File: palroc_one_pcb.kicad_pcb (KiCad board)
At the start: 6 copper layers, 1 part, among them U1 ME54BS13_V1.0

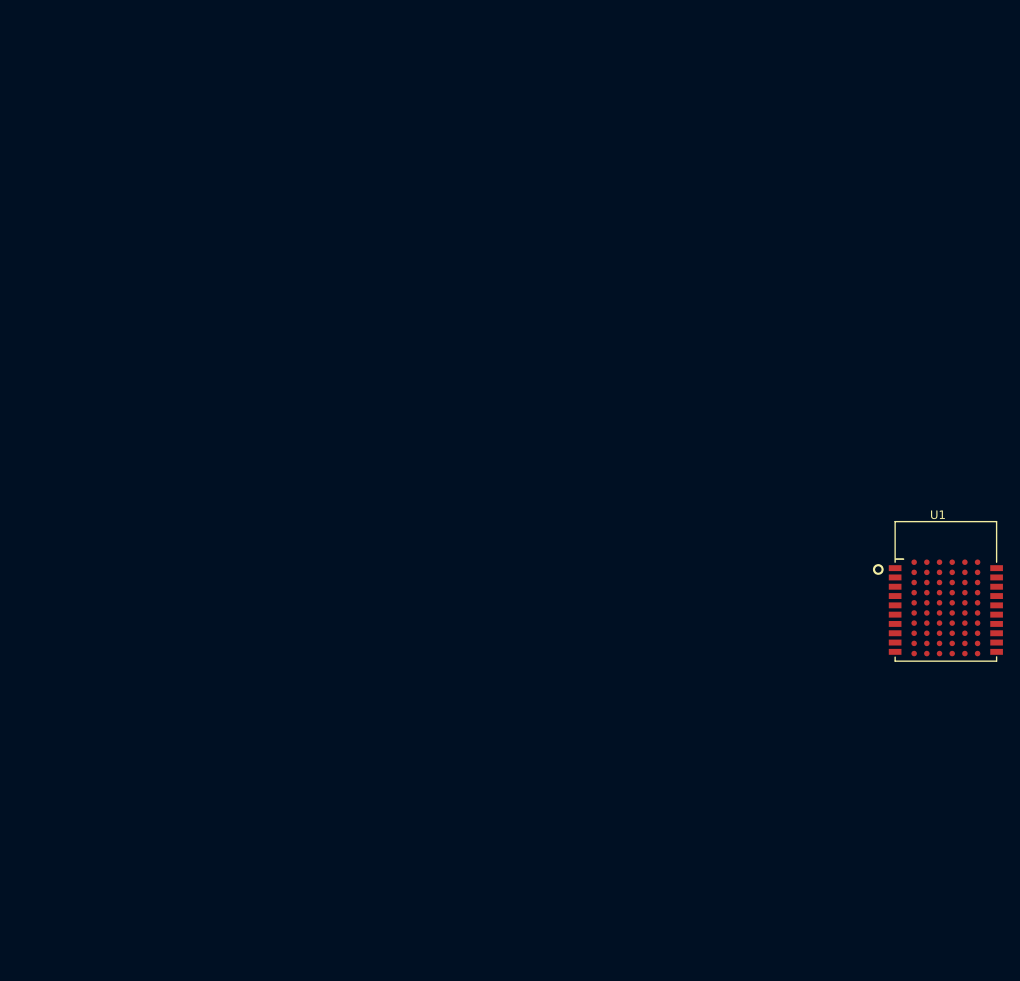
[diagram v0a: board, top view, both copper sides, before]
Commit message: Add power supply, connectors, LoRa, gas sensor, audio, and display sheets
Adds nPM1300 power management, USB-C connectors, Minew LoRa module,
multi-gas sensing (CO2/particulate), audio, and display schematics
along with the supporting component libraries and updated PCB routing.

Co-Authored-By: Claude Sonnet 5 <noreply@anthropic.com>
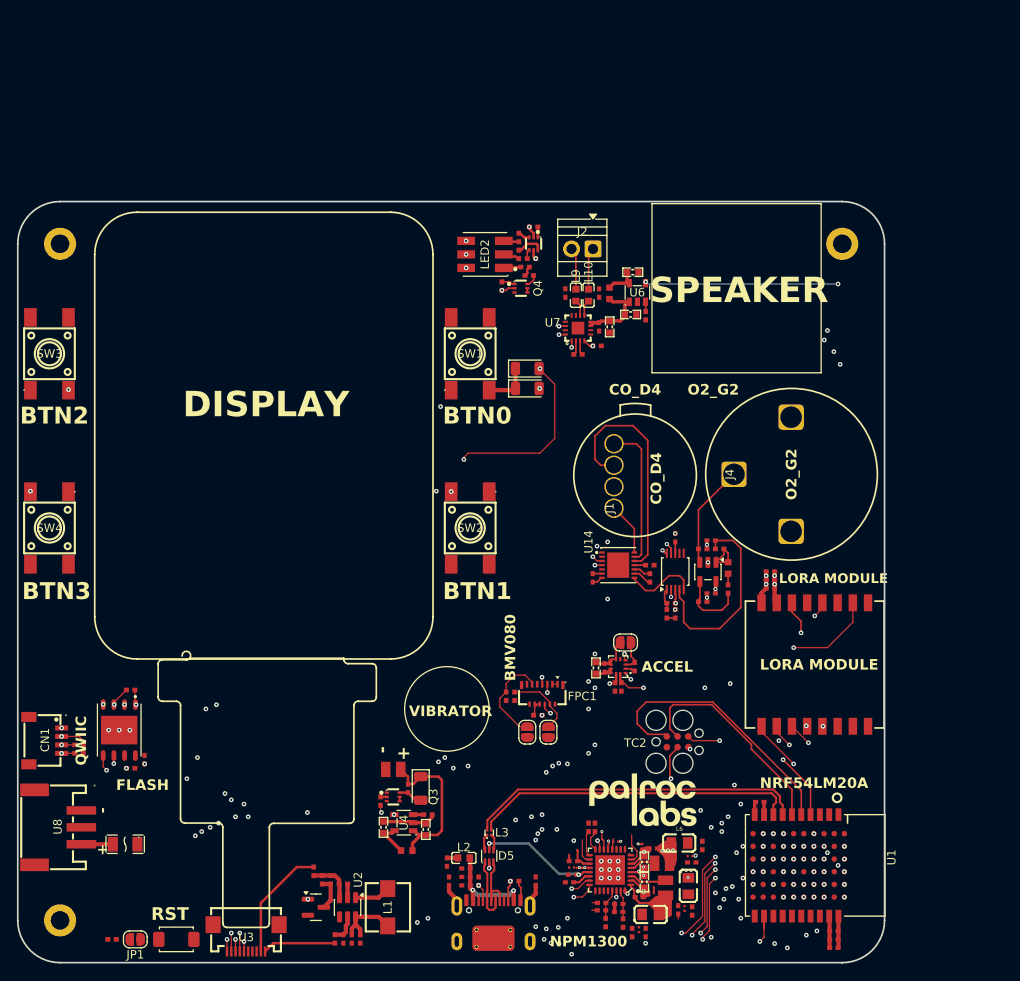
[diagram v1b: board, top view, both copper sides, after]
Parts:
- added C1: 10nF, caps_nordic:c_0402_nordic, F.Cu at (135.2, 128.2)
- added C10: 10nF, caps_nordic:c_0402_nordic, F.Cu at (89.8, 122.4)
- added C11: 10nF, caps_nordic:c_0402_nordic, F.Cu at (91.8, 122.9)
- added C12: 100nF, caps_nordic:c_0402_nordic, F.Cu at (91.8, 121.9)
- added C13: 1uF, caps_nordic:c_0402_nordic, F.Cu at (91.8, 120.9)
- added C14: 100nF, caps_nordic:c_0402_nordic, F.Cu at (89.5, 120.1)
- added C15: 1uF, caps_nordic:c_0402_nordic, F.Cu at (104.3, 121.6)
- added C16: 2.2uF, caps_nordic:c_0402_nordic, F.Cu at (104.5, 120.0)
- added C17: 100nF, caps_nordic:c_0201_nordic, F.Cu at (109.5, 117.7)
- added C18: 10uF, caps_nordic:c_0603_nordic, F.Cu at (112.8, 122.5)
- added C19: 10uF, caps_nordic:c_0402_nordic, F.Cu at (109.8, 125.1)
- added C2: 100nF, caps_nordic:c_0402_nordic, F.Cu at (135.2, 129.2)
- added C20: 1nF, caps_nordic:c_0201_nordic, F.Cu at (113.7, 123.7)
- added C21: 10uF, caps_nordic:c_0402_nordic, F.Cu at (112.2, 124.3)
- added C22: 10uF, caps_nordic:c_0402_nordic, F.Cu at (113.9, 118.5)
- added C23: 10uF, caps_nordic:c_0402_nordic, F.Cu at (109.8, 126.0)
- added C24: 10uF, caps_nordic:c_0603_nordic, F.Cu at (112.8, 120.1)
- added C25: 1nF, caps_nordic:c_0201_nordic, F.Cu at (112.6, 118.3)
- added C26: 1nF, caps_nordic:c_0201_nordic, F.Cu at (104.2, 120.8)
- added C27: 10uF, caps_nordic:c_0402_nordic, F.Cu at (107.8, 124.9)
- added C28: 10uF, caps_nordic:c_0402_nordic, F.Cu at (113.0, 128.5)
- added C29: 10uF, caps_nordic:c_0402_nordic, F.Cu at (118.5, 120.2)
- added C3: 1uF, caps_nordic:c_0402_nordic, F.Cu at (135.2, 130.2)
- added C30: 10uF, caps_nordic:c_0402_nordic, F.Cu at (116.8, 125.8)
- added C31: 10uF, caps_nordic:c_0402_nordic, F.Cu at (107.8, 125.8)
- added C32: 100pF, caps_nordic:c_0201_nordic, F.Cu at (112.2, 128.1)
- added C33: 100pF, caps_nordic:c_0201_nordic, F.Cu at (117.6, 125.6)
- added C34: 100pF, caps_nordic:c_0201_nordic, F.Cu at (118.2, 119.4)
- added C35: 1uF, caps_nordic:c_0402_nordic, F.Cu at (104.0, 122.5)
- added C36: 10uF, caps_nordic:c_0603_nordic, F.Cu at (108.8, 56.8)
- added C37: 100nF, caps_nordic:c_0402_nordic, F.Cu at (107.5, 56.8)
- added C38: 220pF, caps_nordic:c_0402_nordic, F.Cu at (103.5, 52.8)
- added C39: 220pF, caps_nordic:c_0402_nordic, F.Cu at (107.5, 52.8)
- added C4: 10nF, caps_nordic:c_0402_nordic, F.Cu at (127.8, 87.8)
- added C40: 100nF, caps_nordic:c_0402_nordic, F.Cu at (84.9, 111.4)
- added C41: 1uF, caps_nordic:c_0402_nordic, F.Cu at (126.5, 113.0)
- added C42: 100nF, caps_nordic:c_0402_nordic, F.Cu at (53.8, 108.0)
- added C43: 10uF, caps_nordic:c_0603_nordic, F.Cu at (82.0, 116.0)
- added C44: 10uF, caps_nordic:c_0603_nordic, F.Cu at (87.0, 116.2)
- added C45: 10uF, caps_nordic:c_0603_nordic, F.Cu at (111.5, 50.4)
- added C46: 10uF, caps_nordic:c_0603_nordic, F.Cu at (111.2, 55.4)
- added C47: 10uF, caps_nordic:c_0603_nordic, F.Cu at (107.1, 97.1)
- added C48: 100nF, caps_nordic:c_0402_nordic, F.Cu at (108.1, 97.1)
- added C49: 100nF, caps_nordic:c_0402_nordic, F.Cu at (116.5, 81.8)
- added C5: 100nF, caps_nordic:c_0402_nordic, F.Cu at (127.8, 86.8)
- added C50: 100nF, caps_nordic:c_0402_nordic, F.Cu at (120.8, 88.3)
- added C51: 100nF, caps_nordic:c_0402_nordic, F.Cu at (106.8, 86.5)
- added C52: 100nF, caps_nordic:c_0402_nordic, F.Cu at (120.8, 82.1)
- added C6: 1uF, caps_nordic:c_0402_nordic, F.Cu at (127.8, 85.8)
- added C7: 1uF, caps_nordic:c_0402_nordic, F.Cu at (78.2, 129.2)
- added C8: 220pF, caps_nordic:c_0402_nordic, F.Cu at (77.2, 129.2)
- added C9: 10nF, caps_nordic:c_0402_nordic, F.Cu at (100.0, 122.4)
- added CN1: SM04B-SRSS-TB, PALROC_Connectorss:CONN-SMD_4P-P1.00_SM04B-SRSS-TB-LF-SN, F.Cu at (42.0, 105.8)
- added D2: 1N4001W, PCM_JLCPCB:D_SOD-123FL, F.Cu at (86.4, 111.4)
- added D3: 1N4001W, PCM_JLCPCB:D_SOD-123FL, F.Cu at (99.0, 61.8)
- added D4: 1N4001W, PCM_JLCPCB:D_SOD-123FL, F.Cu at (99.0, 64.1)
- added D5: USBLC6-2P6, PALROC-Protection:SOT-666-6_L1.6-W1.2-P0.50-LS1.6-BR, F.Cu at (94.5, 119.4)
- added FPC1: 046844713002846+_C5857733, PALROC_Connectorss:FPC-SMD_13P-P0.60_046844713002846-1, F.Cu at (100.8, 100.3)
- added G***: LOGO, PALROC_Logos:Palroc_Logo_15x15mm, F.Cu at (112.8, 112.8)
- added H1: MountingHole_Pad, MountingHole:MountingHole_2.2mm_M2_DIN965_Pad, F.Cu at (136.2, 47.0)
- added H2: MountingHole_Pad, MountingHole:MountingHole_2.2mm_M2_DIN965_Pad, F.Cu at (43.8, 127.0)
- added H3: MountingHole_Pad, MountingHole:MountingHole_2.2mm_M2_DIN965_Pad, F.Cu at (43.8, 47.0)
- added J1: Conn_01x04, Connector_GasSensors:0294-0-15-80-06-80-10-0_co-d4, F.Cu at (109.2, 78.3)
- added J2: Screw_Terminal_01x02, TerminalBlock:TerminalBlock_Xinya_XY308-2.54-2P_1x02_P2.54mm_Horizontal, F.Cu at (106.8, 47.6)
- added J3: Connector, USB-TYPE-C-16P, PCM_JLCPCB:TYPE-C-SMD_HX-TYPE-C-16PIN, F.Cu at (95.0, 127.1)
- added J4: Conn_01x03, Connector_GasSensors:0364-0-15-80-13-80-10-0_o2-g2, F.Cu at (123.5, 74.2)
- added JP1: SolderJumper_2_Open, Jumper:SolderJumper-2_P1.3mm_Open_RoundedPad1.0x1.5mm, F.Cu at (52.6, 129.2)
- added JP2: SolderJumper_2_Open, Jumper:SolderJumper-2_P1.3mm_Open_RoundedPad1.0x1.5mm, F.Cu at (101.5, 104.8)
- added JP3: SolderJumper_2_Open, Jumper:SolderJumper-2_P1.3mm_Open_RoundedPad1.0x1.5mm, F.Cu at (99.0, 104.8)
- added JP4: SolderJumper_2_Open, Jumper:SolderJumper-2_P1.3mm_Open_RoundedPad1.0x1.5mm, F.Cu at (110.6, 94.1)
- added L1: CXP0530-220M-AG(22UH), PALROC-inductors:IND-SMD_L5.7-W5.2, F.Cu at (82.5, 125.5)
- added L10: BLM18PG471SN1D, PALROC-ferrite-bread:L0603, F.Cu at (106.2, 53.1)
- added L2: BLM18KG121TN1D, PALROC-ferrite-bread:L0603, F.Cu at (91.5, 119.6)
- added L3: DLM0NSN900HY2D, PALROC-Filters:FILTER-SMD_4P-L0.9-W0.7-P0.50-BL-CW, F.Cu at (94.5, 116.6)
- added L4: 2.2uH, l_nordic:l_0806_nordic, F.Cu at (115.3, 123.2)
- added L5: 2.2uH, l_nordic:l_0806_nordic, F.Cu at (115.0, 120.3)
- added L6: BLM21AG102SN1D, PALROC-ferrite-bread:L0805, F.Cu at (117.0, 117.9)
- added L7: BLM21AG102SN1D, PALROC-ferrite-bread:L0805, F.Cu at (113.5, 126.3)
- added L8: BLM21AG102SN1D, PALROC-ferrite-bread:L0805, F.Cu at (118.0, 123.0)
- added L9: BLM18PG471SN1D, PALROC-ferrite-bread:L0603, F.Cu at (104.8, 53.1)
- added LED2: XL-5050RGBC, PALROC-LED:LED-ARRAY-SMD_6P-L5.0-W5.0-TL-RD_3, F.Cu at (94.0, 48.2)
- added M1: MS21SF1_V1.0, minew:MS21SF1_V1.0, F.Cu at (133.0, 96.8)
- added NT1: NetTie_2, PALROC-net_ties:NetTie-PALROC-viamm, F.Cu at (112.9, 119.0)
- added NT2: NetTie_2, PALROC-net_ties:NetTie-PALROC-viamm, F.Cu at (112.8, 123.6)
- added Q1: AO3400A, PCM_JLCPCB:Q_SOT-23, F.Cu at (74.0, 125.5)
- added Q3: SSM6N56FE,LM, PALROC-mosfet:ES6_L1.6-W1.2-P0.50-LS1.6-BL, F.Cu at (83.2, 112.4)
- added Q4: SSM6N56FE,LM, PALROC-mosfet:ES6_L1.6-W1.2-P0.50-LS1.6-BL, F.Cu at (98.2, 52.2)
- added Q5: SSM6N56FE,LM, PALROC-mosfet:ES6_L1.6-W1.2-P0.50-LS1.6-BL, F.Cu at (99.8, 47.0)
- added R1: 0, res_nordic:r_0402_nordic, F.Cu at (79.2, 129.2)
- added R10: 300k, res_nordic:r_0402_nordic, F.Cu at (107.0, 116.0)
- added R11: 300k, res_nordic:r_0402_nordic, F.Cu at (106.2, 116.0)
- added R12: R, res_nordic:r_0603_nordic, F.Cu at (108.7, 52.9)
- added R13: 0, res_nordic:r_0402_nordic, F.Cu at (110.3, 127.3)
- added R14: 0, res_nordic:r_0402_nordic, F.Cu at (108.3, 127.3)
- added R15: 0, res_nordic:r_0402_nordic, F.Cu at (118.5, 125.9)
- added R16: 0, res_nordic:r_0402_nordic, F.Cu at (111.4, 128.5)
- added R17: 0, res_nordic:r_0402_nordic, F.Cu at (119.7, 118.2)
- added R18: 1Meg, res_nordic:r_0402_nordic, F.Cu at (107.2, 59.1)
- added R19: 100k, res_nordic:r_0402_nordic, F.Cu at (105.0, 60.1)
- added R2: 47, res_nordic:r_0402_nordic, F.Cu at (77.2, 122.7)
- added R20: 1Meg, res_nordic:r_0402_nordic, F.Cu at (81.7, 112.9)
- added R21: 5.1k, res_nordic:r_0402_nordic, F.Cu at (52.1, 99.8)
- added R22: 5.1k, res_nordic:r_0402_nordic, F.Cu at (87.2, 114.5)
- added R23: 100k, res_nordic:r_0402_nordic, F.Cu at (49.9, 129.2)
- added R24: 1Meg, res_nordic:r_0402_nordic, F.Cu at (96.0, 52.0)
- added R25: 0, res_nordic:r_0402_nordic, F.Cu at (52.1, 109.0)
- added R26: 1Meg, res_nordic:r_0402_nordic, F.Cu at (99.8, 45.0)
- added R27: 1Meg, res_nordic:r_0402_nordic, F.Cu at (99.5, 48.8)
- added R28: 100, res_nordic:r_0402_nordic, F.Cu at (98.8, 49.8)
- added R29: 100, res_nordic:r_0402_nordic, F.Cu at (99.2, 50.8)
- added R3: 0, res_nordic:r_0402_nordic, F.Cu at (76.2, 129.2)
- added R30: 5.1k, res_nordic:r_0402_nordic, F.Cu at (113.0, 55.5)
- added R31: 100, res_nordic:r_0402_nordic, F.Cu at (98.0, 48.2)
- added R32: 100, res_nordic:r_0402_nordic, F.Cu at (98.0, 46.2)
- added R33: R, l_nordic:l_0806_nordic, F.Cu at (83.2, 109.2)
- added R34: 5.1k, res_nordic:r_0402_nordic, F.Cu at (96.5, 100.5)
- added R35: 5.1k, res_nordic:r_0402_nordic, F.Cu at (97.5, 100.5)
- added R36: 5.1k, res_nordic:r_0402_nordic, F.Cu at (100.2, 102.8)
- added R37: 100k, res_nordic:r_0402_nordic, F.Cu at (111.7, 97.0)
- added R38: 100k, res_nordic:r_0402_nordic, F.Cu at (110.1, 99.4)
- added R39: 100k, res_nordic:r_0402_nordic, F.Cu at (109.4, 99.4)
- added R4: 10, res_nordic:r_0402_nordic, F.Cu at (74.8, 122.2)
- added R40: 5.1k, res_nordic:r_0402_nordic, F.Cu at (46.0, 107.2)
- added R41: 5.1k, res_nordic:r_0402_nordic, F.Cu at (46.0, 106.2)
- added R42: 5.1k, res_nordic:r_0402_nordic, F.Cu at (116.5, 90.8)
- added R43: 0, res_nordic:r_0402_nordic, F.Cu at (115.5, 90.8)
- added R44: 0, res_nordic:r_0402_nordic, F.Cu at (116.0, 89.5)
- added R45: 100, res_nordic:r_0402_nordic, F.Cu at (119.8, 83.1)
- added R46: 1k, res_nordic:r_0402_nordic, F.Cu at (119.8, 89.3)
- added R47: 0, res_nordic:r_0402_nordic, F.Cu at (113.5, 86.5)
- added R48: 300k, res_nordic:r_0402_nordic, F.Cu at (122.8, 87.8)
- added R5: 10, res_nordic:r_0402_nordic, F.Cu at (75.8, 122.2)
- added R50: 0, res_nordic:r_0402_nordic, F.Cu at (113.5, 85.0)
- added R51: 47k, res_nordic:r_0402_nordic, F.Cu at (121.8, 83.1)
- added R52: 30k, res_nordic:r_0603_nordic, F.Cu at (122.8, 85.3)
- added R6: 0, res_nordic:r_0402_nordic, F.Cu at (73.8, 121.2)
- added R7: 5.1k, res_nordic:r_0402_nordic, F.Cu at (93.2, 122.4)
- added R8: 5.1k, res_nordic:r_0402_nordic, F.Cu at (97.5, 122.4)
- added R9: R, res_nordic:r_0603_nordic, F.Cu at (84.8, 118.8)
- added S1: Tactile Button, 160gf, PCM_JLCPCB:SW_TS-1088-AR02016, F.Cu at (57.5, 129.2)
- added SW1: ZX-QC66-8.5TP, PALROC-Buttons:KEY-SMD_4P-L6.0-W6.0-P4.50-LS8.6_H8.5, F.Cu at (92.2, 60.0)
- added SW2: ZX-QC66-8.5TP, PALROC-Buttons:KEY-SMD_4P-L6.0-W6.0-P4.50-LS8.6_H8.5, F.Cu at (92.2, 80.6)
- added SW3: ZX-QC66-8.5TP, PALROC-Buttons:KEY-SMD_4P-L6.0-W6.0-P4.50-LS8.6_H8.5, F.Cu at (42.5, 60.0)
- added SW4: ZX-QC66-8.5TP, PALROC-Buttons:KEY-SMD_4P-L6.0-W6.0-P4.50-LS8.6_H8.5, F.Cu at (42.5, 80.6)
- added TC2: TC2030-IDC, PALROC_Connectors:TC2030-IDC, F.Cu at (116.8, 105.9)
- added U10: MF-NSMF200-2, PALROC-fuse:F1206, F.Cu at (51.5, 118.0)
- added U11: LIS2DW12TR, PALROC_MotionSensors:LGA-12_L2.0-W2.0-P0.50-BL, F.Cu at (109.8, 97.0)
- added U12: ADS1115IDGS, PCM_JLCPCB:TSSOP-10_3x3mm_P0.5mm, F.Cu at (116.5, 85.8)
- added U13: OPA333xxDBV, Package_TO_SOT_SMD:SOT-23-5, F.Cu at (120.4, 85.8)
- added U14: LMP91000SDX/NOPB, PALROC-GasSensors:WSON-14_L4.0-W4.0-P0.50-BL-EP-1, F.Cu at (109.8, 85.0)
- added U2: AP3019AKTR, Package_TO_SOT_SMD:SOT-23-6, F.Cu at (77.8, 125.5)
- added U3: FPC 0.5-10P HYH2.0, PALROC_Connectors:FPC-SMD_10P-P0.50_FPC-0.5-10P-HYH2.0, F.Cu at (65.8, 129.1)
- added U4: MT9700-N, PALROC-pmic:SOT-23-5_L2.9-W1.6-P0.95-LS2.9-BL, F.Cu at (84.4, 115.5)
- added U5: nPM1300-QEAA, npm1300:Nordic_QFN50P500X500X90-33N, F.Cu at (108.8, 121.1)
- added U6: MT9700-N, PALROC-pmic:SOT-23-5_L2.9-W1.6-P0.95-LS2.9-BL, F.Cu at (112.0, 52.8)
- added U7: MAX98357AETE+T, PALROC-Audio:TQFN-16_L3.0-W3.0-P0.50-BL-EP1.5, F.Cu at (105.0, 57.0)
- added U8: S3B-PH-SM4-TB, PALROC_Connectors:CONN-SMD_S3B-PH-SM4-TB-LF-SN, F.Cu at (43.5, 116.0)
- added U9: W25Q128JVPIQTR, PALROC-nor-flash:WSON-8_L6.0-W5.0-P1.27-BL-EP, F.Cu at (50.8, 104.5)
- moved U1 25.4 mm to (124.8, 114.5), turned to -90 degrees
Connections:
- U1 pad 1: unconnected-(U1E-GND-Pad1) -> GND
- U1 pad 10: unconnected-(U1E-GND-Pad10) -> GND
- U1 pad 11: unconnected-(U1E-GND-Pad11) -> GND
- U1 pad 12: unconnected-(U1B-P1.26-Pad12) -> /Project Architecture/Misc/BTN_0
- U1 pad 16: unconnected-(U1B-P1.17-Pad16) -> /Project Architecture/NRF54LM20A/UART_RX
- U1 pad 17: unconnected-(U1B-P1.16-Pad17) -> /Project Architecture/NRF54LM20A/UART_TX
- U1 pad 19: unconnected-(U1E-VCC-Pad19) -> +3V3
- U1 pad 20: unconnected-(U1E-GND-Pad20) -> GND
- U1 pad 3: unconnected-(U1E-GND-Pad3) -> GND
- U1 pad 4: unconnected-(U1E-nRESET-Pad4) -> /Project Architecture/Connectors/RST_NRF54
- U1 pad 5: unconnected-(U1E-SWDIO-Pad5) -> /Project Architecture/Connectors/SWDIO_NRF54
- U1 pad 6: unconnected-(U1E-SWDCLK-Pad6) -> /Project Architecture/Connectors/SWDCLK_NRF54
- U1 pad 7: unconnected-(U1E-D--Pad7) -> /Project Architecture/Connectors/D1_N
- U1 pad 8: unconnected-(U1E-D+-Pad8) -> /Project Architecture/Connectors/D1_P
- U1 pad 9: unconnected-(U1E-VBUS-Pad9) -> VBUS_out
- U1 pad A3: unconnected-(U1D-P3.04-PadA3) -> /Project Architecture/LORA/LORA_SCK
- U1 pad A6: unconnected-(U1B-P1.06/AIN4-PadA6) -> /Project Architecture/DISPLAY/DISP_RST
- U1 pad A7: unconnected-(U1B-P1.00/AIN0-PadA7) -> /Project Architecture/DISPLAY/DISP_MOSI
- U1 pad A8: unconnected-(U1B-P1.04/AIN6-PadA8) -> /Project Architecture/DISPLAY/DISP_CS
- U1 pad B0: unconnected-(U1A-P0.02-PadB0) -> /Project Architecture/Misc/AUD_ENABLE
- U1 pad B2: unconnected-(U1D-P3.03-PadB2) -> /Project Architecture/Misc/I2S_BCLK
- U1 pad B3: unconnected-(U1D-P3.02-PadB3) -> /Project Architecture/LORA/LORA_DIO1
- U1 pad B4: unconnected-(U1D-P3.01-PadB4) -> /Project Architecture/LORA/LORA_BUSY
- U1 pad B5: unconnected-(U1D-P3.00-PadB5) -> /Project Architecture/LORA/LORA_RST
- U1 pad B6: unconnected-(U1B-P1.07/EXTREF-PadB6) -> /Project Architecture/Connectors/I2C_SDA
- U1 pad B8: unconnected-(U1B-P1.03/AIN7-PadB8) -> /Project Architecture/DISPLAY/DISP_SCK
- U1 pad C0: unconnected-(U1A-P0.05-PadC0) -> /Project Architecture/Misc/BTN_3
- U1 pad C2: unconnected-(U1D-P3.07-PadC2) -> /Project Architecture/Misc/AMP_SD
- U1 pad C3: unconnected-(U1D-P3.08-PadC3) -> /Project Architecture/LORA/LORA_MOSI
- U1 pad C4: unconnected-(U1D-P3.06-PadC4) -> /Project Architecture/Misc/I2S_DIN
- U1 pad C5: unconnected-(U1D-P3.05-PadC5) -> /Project Architecture/Misc/I2S_LRCLK
- U1 pad C6: unconnected-(U1B-P1.08-PadC6) -> /Project Architecture/Misc/BTN_2
- U1 pad C7: unconnected-(U1B-P1.05/AIN5-PadC7) -> /Project Architecture/DISPLAY/DISP_DC
- U1 pad C8: unconnected-(U1C-P2.04-PadC8) -> /Project Architecture/Misc/SPI_MISO
- U1 pad D0: unconnected-(U1E-GND-PadD0) -> GND
- U1 pad D2: unconnected-(U1D-P3.11-PadD2) -> /Project Architecture/Misc/VIB_PWM
- U1 pad D3: unconnected-(U1D-P3.10-PadD3) -> /Project Architecture/LORA/LORA_NSS
- U1 pad D5: unconnected-(U1D-P3.09-PadD5) -> /Project Architecture/LORA/LORA_MISO
- U1 pad D6: unconnected-(U1B-P1.09-PadD6) -> /Project Architecture/Misc/BTN_1
- U1 pad D8: unconnected-(U1C-P2.05-PadD8) -> /Project Architecture/Misc/SPI_EXT_MEM_CS
- U1 pad D9: unconnected-(U1C-P2.02-PadD9) -> /Project Architecture/Misc/SPI_MOSI
- U1 pad E0: unconnected-(U1E-GND-PadE0) -> GND
- U1 pad E2: unconnected-(U1D-P3.12-PadE2) -> /Project Architecture/Misc/VIB_ENABLE
- U1 pad E3: unconnected-(U1B-P1.10-PadE3) -> /Project Architecture/DISPLAY/DISP_DIM
- U1 pad E4: unconnected-(U1B-P1.22-PadE4) -> /Project Architecture/Misc/LED1_R
- U1 pad E5: unconnected-(U1B-P1.25-PadE5) -> /Project Architecture/Misc/LED1_G
- U1 pad E7: unconnected-(U1C-P2.09-PadE7) -> /Project Architecture/Connectors/SWO_NRF54
- U1 pad E9: unconnected-(U1C-P2.01-PadE9) -> /Project Architecture/Misc/SPI_SCK
- U1 pad F0: unconnected-(U1E-GND-PadF0) -> GND
- U1 pad F2: unconnected-(U1B-P1.14-PadF2) -> /Project Architecture/Misc/INT1_ACCEL
- U1 pad F3: unconnected-(U1B-P1.13-PadF3) -> /Project Architecture/Connectors/I2C_SCL
- U1 pad F4: unconnected-(U1B-P1.12-PadF4) -> /Project Architecture/Misc/INT2_ACCEL
- U1 pad F5: unconnected-(U1B-P1.11-PadF5) -> /Project Architecture/LORA/LORA_ANT_SW
- U1 pad F6: unconnected-(U1B-P1.27-PadF6) -> /Project Architecture/Misc/LED1_B
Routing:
- net /Project Architecture/Misc/BTN_2: track 0.00 -> 162.0 mm, vias 0 -> 7
- net /Project Architecture/Connectors/I2C_SCL: track 0.00 -> 156.7 mm, vias 0 -> 13
- net /Project Architecture/Misc/BTN_3: track 0.00 -> 152.5 mm, vias 0 -> 8
- net /Project Architecture/Connectors/I2C_SDA: track 0.00 -> 144.2 mm, vias 0 -> 11
- net /Project Architecture/Misc/BTN_0: track 0.00 -> 118.1 mm, vias 0 -> 6
- net /Project Architecture/Misc/LED1_R: track 0.00 -> 112.4 mm, vias 0 -> 5
- net /Project Architecture/Misc/SPI_MISO: track 0.00 -> 109.6 mm, vias 0 -> 8
- net /Project Architecture/Misc/SPI_EXT_MEM_CS: track 0.00 -> 109.4 mm, vias 0 -> 8
- net /Project Architecture/Misc/LED1_G: track 0.00 -> 106.0 mm, vias 0 -> 5
- net /Project Architecture/Misc/SPI_SCK: track 0.00 -> 105.2 mm, vias 0 -> 8
- net /Project Architecture/Misc/LED1_B: track 0.00 -> 104.6 mm, vias 0 -> 5
- net /Project Architecture/Misc/SPI_MOSI: track 0.00 -> 103.4 mm, vias 0 -> 8
- net /Project Architecture/Misc/BTN_1: track 0.00 -> 100.6 mm, vias 0 -> 6
- net /Project Architecture/Misc/I2S_LRCLK: track 0.00 -> 99.1 mm, vias 0 -> 4
- net /Project Architecture/Misc/I2S_DIN: track 0.00 -> 97.1 mm, vias 0 -> 4
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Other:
- board outline added: 102.5 x 90 mm
- board text added: "+ -"
- board text added: "ACCEL"
- board text added: "BMV080"
- board text added: "BTN0"
- board text added: "BTN1"
- board text added: "BTN2"
- board text added: "BTN3"
- board text added: "CO_D4"
- board text added: "DISPLAY"
- board text added: "FLASH"
- board text added: "LORA MODULE"
- board text added: "NPM1300"
- board text added: "NRF54LM20A"
- board text added: "O2_G2"
- board text added: "QWIIC"
- board text added: "RST"
- board text added: "SPEAKER"
- board text added: "VIBRATOR"

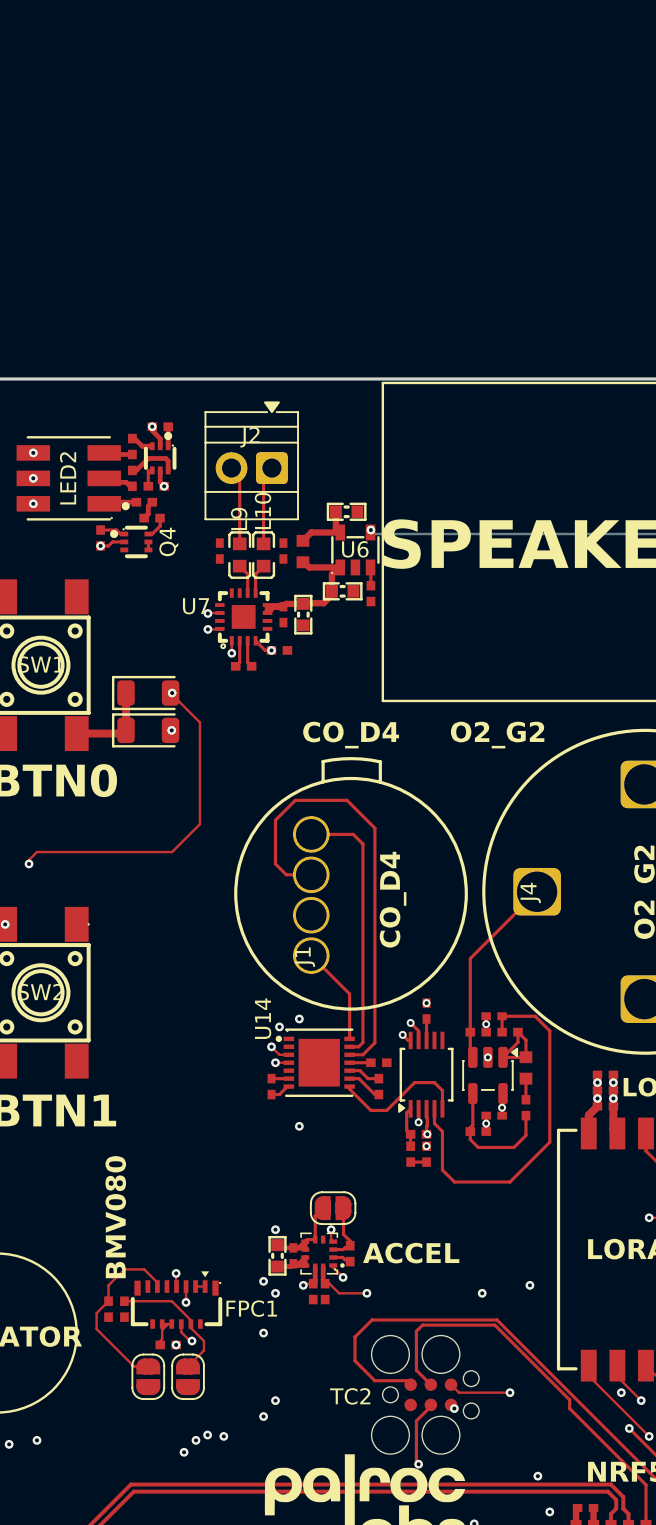
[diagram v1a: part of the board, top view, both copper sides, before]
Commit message: Update footprint 3D models, add through-hole connector, and refine PCB layout
Refreshes 3D shapes/step models across several component libraries,
adds a new XY308 2.54mm through-hole connector footprint, and updates
PCB placement/routing and CI workflow.

Co-Authored-By: Claude Sonnet 5 <noreply@anthropic.com>
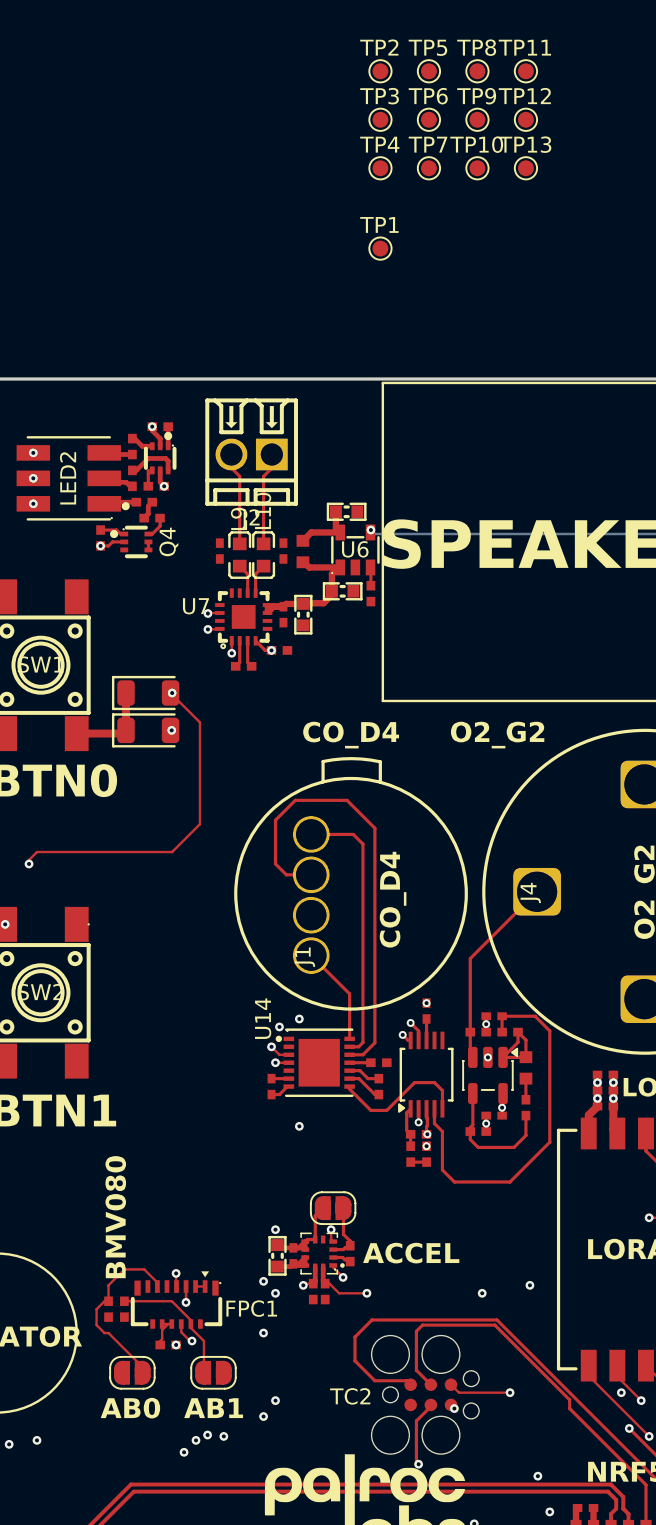
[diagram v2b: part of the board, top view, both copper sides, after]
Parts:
- added TP1: TestPoint_Probe, TestPoint:TestPoint_Pad_D1.0mm, F.Cu at (113.6, 33.8)
- added TP10: TestPoint_Probe, TestPoint:TestPoint_Pad_D1.0mm, F.Cu at (119.7, 28.8)
- added TP11: TestPoint_Probe, TestPoint:TestPoint_Pad_D1.0mm, F.Cu at (122.8, 22.6)
- added TP12: TestPoint_Probe, TestPoint:TestPoint_Pad_D1.0mm, F.Cu at (122.8, 25.7)
- added TP13: TestPoint_Probe, TestPoint:TestPoint_Pad_D1.0mm, F.Cu at (122.8, 28.8)
- added TP2: TestPoint_Probe, TestPoint:TestPoint_Pad_D1.0mm, F.Cu at (113.6, 22.6)
- added TP3: TestPoint_Probe, TestPoint:TestPoint_Pad_D1.0mm, F.Cu at (113.6, 25.7)
- added TP4: TestPoint_Probe, TestPoint:TestPoint_Pad_D1.0mm, F.Cu at (113.6, 28.8)
- added TP5: TestPoint_Probe, TestPoint:TestPoint_Pad_D1.0mm, F.Cu at (116.7, 22.6)
- added TP6: TestPoint_Probe, TestPoint:TestPoint_Pad_D1.0mm, F.Cu at (116.7, 25.7)
- added TP7: TestPoint_Probe, TestPoint:TestPoint_Pad_D1.0mm, F.Cu at (116.7, 28.8)
- added TP8: TestPoint_Probe, TestPoint:TestPoint_Pad_D1.0mm, F.Cu at (119.7, 22.6)
- added TP9: TestPoint_Probe, TestPoint:TestPoint_Pad_D1.0mm, F.Cu at (119.7, 25.7)
- J2: footprint TerminalBlock:TerminalBlock_Xinya_XY308-2.54-2P_1x02_P2.54mm_Horizontal -> PALROC_Connectorss:CONN-TH_XY308-2.54-2P
- moved JP2 1.62 mm to (103.1, 104.5), turned to 180 degrees
- moved J2 1.53 mm to (105.5, 46.8)
- moved JP3 1.03 mm to (98.0, 104.5), turned to 0 degrees
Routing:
- net /Project Architecture/Misc/AB0: track 11.4 -> 12.0 mm
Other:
- board text added: "AB0"
- board text added: "AB1"
